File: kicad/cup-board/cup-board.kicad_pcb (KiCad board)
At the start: 4 copper layers, 0 parts

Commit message: [LIMA] cup PCB: ring outline (62/38 mm, centre 150,100), JLC 4-layer rules, netclasses
Outline drawn with KiCad's pcbnew API (Konnect has no circular Edge.Cuts
tool); DRC on the saved file: 0 violations.

Co-Authored-By: Claude Opus 5.5 <noreply@anthropic.com>
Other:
- board outline added: 62 x 62 mm
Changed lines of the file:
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@@
 (kicad_pcb
-	(version 20250610)
-	(generator "konnect")
+	(version 20260206)
+	(generator "pcbnew")
 	(generator_version "10.0")
 	(general
 		(thickness 1.6)
+		(legacy_teardrops no)
 	)
 	(paper "A4")
 	(layers
 		(0 "F.Cu" signal)
-		(31 "B.Cu" signal)
-		(32 "B.Adhes" user "B.Adhesive")
-		(33 "F.Adhes" user "F.Adhesive")
-		(34 "B.Paste" user)
-		(35 "F.Paste" user)
-		(36 "B.SilkS" user "B.Silkscreen")
-		(37 "F.SilkS" user "F.Silkscreen")
-		(38 "B.Mask" user)
-		(39 "F.Mask" user)
-		(40 "Dwgs.User" user "User.Drawings")
-		(41 "Cmts.User" user "User.Comments")
-		(44 "Edge.Cuts" user)
-		(45 "Margin" user)
-		(46 "B.CrtYd" user "B.Courtyard")
-		(47 "F.CrtYd" user "F.Courtyard")
-		(48 "B.Fab" user)
-		(49 "F.Fab" user)
-		(1 "In1.Cu" power)
-		(2 "In2.Cu" mixed)
+		(4 "In1.Cu" power)
+		(6 "In2.Cu" mixed)
+		(2 "B.Cu" signal)
+		(9 "F.Adhes" user "F.Adhesive")
+		(11 "B.Adhes" user "B.Adhesive")
+		(13 "F.Paste" user)
+		(15 "B.Paste" user)
+		(5 "F.SilkS" user "F.Silkscreen")
+		(7 "B.SilkS" user "B.Silkscreen")
+		(1 "F.Mask" user)
+		(3 "B.Mask" user)
+		(17 "Dwgs.User" user "User.Drawings")
+		(19 "Cmts.User" user "User.Comments")
+		(25 "Edge.Cuts" user)
+		(27 "Margin" user)
+		(31 "F.CrtYd" user "F.Courtyard")
+		(29 "B.CrtYd" user "B.Courtyard")
+		(35 "F.Fab" user)
+		(33 "B.Fab" user)
 	)
 	(setup
 		(pad_to_mask_clearance 0.05)
+		(allow_soldermask_bridges_in_footprints no)
+		(tenting
+			(front yes)
+			(back yes)
+		)
+		(covering
+			(front no)
+			(back no)
+		)
+		(plugging
+			(front no)
+			(back no)
+		)
+		(capping no)
+		(filling no)
+		(pcbplotparams
+			(layerselection 0x00000000_00000000_55555555_5755f5ff)
+			(plot_on_all_layers_selection 0x00000000_00000000_00000000_00000000)
+			(disableapertmacros no)
+			(usegerberextensions no)
+			(usegerberattributes yes)
+			(usegerberadvancedattributes yes)
+			(creategerberjobfile yes)
+			(dashed_line_dash_ratio 12)
+			(dashed_line_gap_ratio 3)
+			(svgprecision 4)
+			(plotframeref no)
+			(mode 1)
+			(useauxorigin no)
+			(pdf_front_fp_property_popups yes)
+			(pdf_back_fp_property_popups yes)
+			(pdf_metadata yes)
+			(pdf_single_document no)
+			(dxfpolygonmode yes)
+			(dxfimperialunits yes)
+			(dxfusepcbnewfont yes)
+			(psnegative no)
+			(psa4output no)
+			(plot_black_and_white yes)
+			(sketchpadsonfab no)
+			(plotpadnumbers no)
+			(hidednponfab no)
+			(sketchdnponfab yes)
+			(crossoutdnponfab yes)
+			(subtractmaskfromsilk no)
+			(outputformat 1)
+			(mirror no)
+			(drillshape 1)
+			(scaleselection 1)
+			(outputdirectory "")
+		)
 	)
-	(net 0 "")
+	(gr_circle
+		(center 150 100)
+		(end 169 100)
+		(stroke
+			(width 0.05)
+			(type default)
+		)
+		(fill no)
+		(layer "Edge.Cuts")
+	)
+	(gr_circle
+		(center 150 100)
+		(end 181 100)
+		(stroke
+			(width 0.05)
+			(type default)
+		)
+		(fill no)
+		(layer "Edge.Cuts")
+	)
+	(embedded_fonts no)
 )

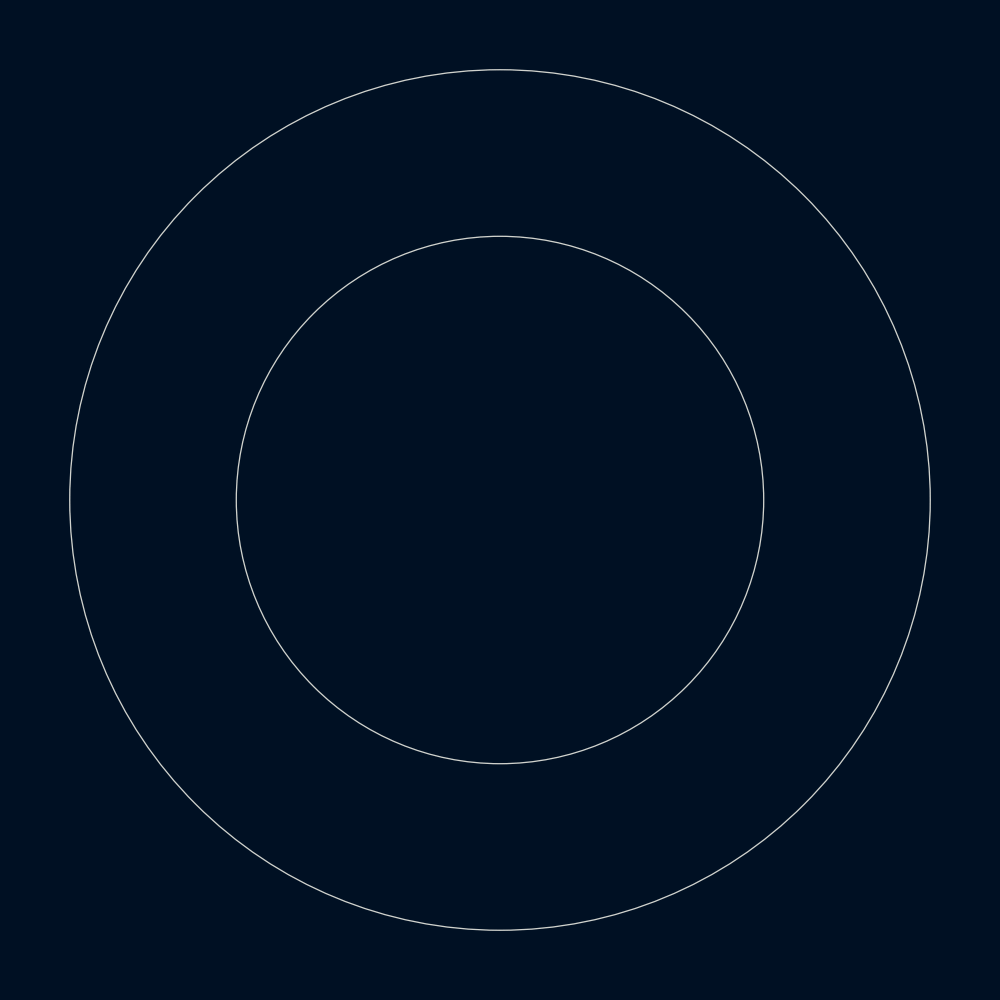
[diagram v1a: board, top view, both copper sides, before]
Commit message: [LIMA] cup PCB: ring enlarged to 68/38 mm (Peter); ring placement plan
62/38 put the parts at 57% courtyard fill on one side; Peter chose the
68/38 ring (single-sided, ~43%). Outer Edge.Cuts circle replaced r31 -> r34
via KiCad's pcbnew API (inner r19 unchanged).

doc/ring_placement.py packs the parts around the ring in signal order
(codec top, K2 right, A2B bottom, power/PPG left, mics upper right) and
checks exact courtyard corners against the ring and every pair for overlap:
359.9 deg used, 0 problems. Placement not yet applied (needs the schematic
sync with KiCad open).

Co-Authored-By: Claude Opus 5.5 <noreply@anthropic.com>
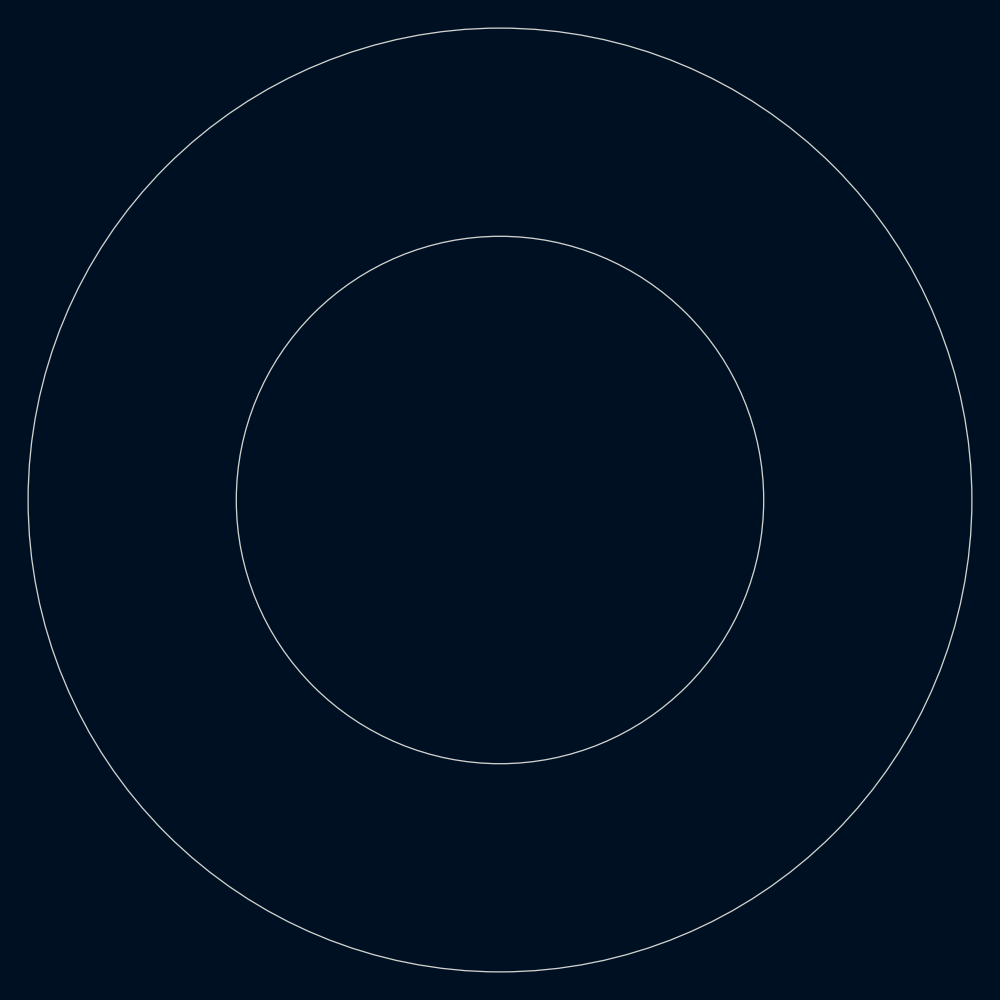
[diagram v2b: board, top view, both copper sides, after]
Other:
- board size 62 x 62 mm -> 68 x 68 mm
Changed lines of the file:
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@@
 	(gr_circle
 		(center 150 100)
-		(end 181 100)
+		(end 184 100)
 		(stroke
 			(width 0.05)

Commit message: [LIMA] cup PCB: 102 footprints synced from schematic (partial placement, pre-script)
Co-Authored-By: Claude Opus 5.5 <noreply@anthropic.com>
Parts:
- added C1: 100nF, Capacitor_SMD:C_0603_1608Metric, F.Cu at (6.48, 0.73)
- added C10: 1uF, Capacitor_SMD:C_0603_1608Metric, F.Cu at (6.48, 59.9)
- added C11: 1uF, Capacitor_SMD:C_0603_1608Metric, F.Cu at (6.48, 66.3)
- added C12: 330nF, Capacitor_SMD:C_0603_1608Metric, F.Cu at (6.48, 72.8)
- added C13: 12pF C0G, Capacitor_SMD:C_0603_1608Metric, F.Cu at (6.48, 79.2)
- added C14: 27pF C0G, Capacitor_SMD:C_0603_1608Metric, F.Cu at (6.48, 85.7)
- added C15: 27pF C0G, Capacitor_SMD:C_0603_1608Metric, F.Cu at (6.48, 92.2)
- added C16: 33nF, Capacitor_SMD:C_0603_1608Metric, F.Cu at (6.48, 98.6)
- added C17: 33nF, Capacitor_SMD:C_0603_1608Metric, F.Cu at (6.48, 105.1)
- added C18: 10nF, Capacitor_SMD:C_0603_1608Metric, F.Cu at (6.48, 111.5)
- added C19: 10nF, Capacitor_SMD:C_0603_1608Metric, F.Cu at (6.48, 118.0)
- added C2: 100nF, Capacitor_SMD:C_0603_1608Metric, F.Cu at (6.48, 7.19)
- added C20: 33nF, Capacitor_SMD:C_0603_1608Metric, F.Cu at (6.48, 124.5)
- added C21: 33nF, Capacitor_SMD:C_0603_1608Metric, F.Cu at (6.48, 130.9)
- added C22: 470nF, Capacitor_SMD:C_0603_1608Metric, F.Cu at (6.48, 137.4)
- added C23: 10uF 16V, Capacitor_SMD:C_0805_2012Metric, F.Cu at (6.70, 144.1)
- added C24: 33nF, Capacitor_SMD:C_0603_1608Metric, F.Cu at (6.48, 150.8)
- added C25: 15nF, Capacitor_SMD:C_0603_1608Metric, F.Cu at (6.48, 157.3)
- added C26: 3.3nF, Capacitor_SMD:C_0603_1608Metric, F.Cu at (6.48, 163.7)
- added C27: 12pF C0G, Capacitor_SMD:C_0603_1608Metric, F.Cu at (6.48, 170.2)
- added C28: 27pF C0G, Capacitor_SMD:C_0603_1608Metric, F.Cu at (6.48, 176.6)
- added C29: 33nF, Capacitor_SMD:C_0603_1608Metric, F.Cu at (6.48, 183.1)
- added C3: 10uF, Capacitor_SMD:C_0805_2012Metric, F.Cu at (6.70, 13.9)
- added C30: 10nF, Capacitor_SMD:C_0603_1608Metric, F.Cu at (6.48, 189.6)
- added C31: 10nF, Capacitor_SMD:C_0603_1608Metric, F.Cu at (6.48, 196.0)
- added C32: 33nF, Capacitor_SMD:C_0603_1608Metric, F.Cu at (6.48, 202.5)
- added C33: 33nF, Capacitor_SMD:C_0603_1608Metric, F.Cu at (6.48, 208.9)
- added C34: 33nF, Capacitor_SMD:C_0603_1608Metric, F.Cu at (6.48, 215.4)
- added C35: 100nF, Capacitor_SMD:C_0603_1608Metric, F.Cu at (6.48, 221.9)
- added C36: 4.7uF, Capacitor_SMD:C_0603_1608Metric, F.Cu at (6.48, 228.3)
- added C37: 100nF, Capacitor_SMD:C_0603_1608Metric, F.Cu at (6.48, 234.8)
- added C38: 4.7uF, Capacitor_SMD:C_0603_1608Metric, F.Cu at (6.48, 241.2)
- added C39: 100nF, Capacitor_SMD:C_0603_1608Metric, F.Cu at (6.48, 247.7)
- added C4: 100nF, Capacitor_SMD:C_0603_1608Metric, F.Cu at (6.48, 20.6)
- added C40: 100nF, Capacitor_SMD:C_0603_1608Metric, F.Cu at (6.48, 254.2)
- added C41: 10uF 16V, Capacitor_SMD:C_0805_2012Metric, F.Cu at (6.70, 260.9)
- added C42: 22uF, Capacitor_SMD:C_0805_2012Metric, F.Cu at (6.70, 267.8)
- added C43: 2.2uF 16V, Capacitor_SMD:C_0603_1608Metric, F.Cu at (6.48, 274.6)
- added C44: 2.2uF, Capacitor_SMD:C_0603_1608Metric, F.Cu at (6.48, 281.0)
- added C45: 2.2uF 16V, Capacitor_SMD:C_0603_1608Metric, F.Cu at (6.48, 287.5)
- added C46: 2.2uF, Capacitor_SMD:C_0603_1608Metric, F.Cu at (6.48, 293.9)
- added C47: 1uF, Capacitor_SMD:C_0603_1608Metric, F.Cu at (6.48, 300.4)
- added C48: 100nF, Capacitor_SMD:C_0603_1608Metric, F.Cu at (6.48, 306.8)
- added C5: 100nF, Capacitor_SMD:C_0603_1608Metric, F.Cu at (6.48, 27.1)
- added C6: 10uF, Capacitor_SMD:C_0805_2012Metric, F.Cu at (6.70, 33.8)
- added C7: 1uF, Capacitor_SMD:C_0603_1608Metric, F.Cu at (6.48, 40.5)
- added C8: 1uF, Capacitor_SMD:C_0603_1608Metric, F.Cu at (6.48, 46.9)
- added C9: 1uF, Capacitor_SMD:C_0603_1608Metric, F.Cu at (6.48, 53.4)
- added D1: ZLLS400, Diode_SMD:D_SOD-323, F.Cu at (131.0, 92.9)
- added FB1: 1000R@100MHz, Inductor_SMD:L_0603_1608Metric, F.Cu at (137.4, 119.5)
- added FB2: 1000R@100MHz, Inductor_SMD:L_0603_1608Metric, F.Cu at (136.5, 120.9)
- added FB3: 1000R@100MHz, Inductor_SMD:L_0603_1608Metric, F.Cu at (130.7, 112.8)
- added FB4: 1000R@100MHz, Inductor_SMD:L_0603_1608Metric, F.Cu at (129.3, 113.7)
- added FL1: 2600R@100MHz CMC, Inductor_SMD:L_CommonModeChoke_Coilank_ACM3216, F.Cu at (142.8, 125.5)
- added FL2: 2600R@100MHz CMC, Inductor_SMD:L_CommonModeChoke_Coilank_ACM3216, F.Cu at (127.3, 110.2)
- added H1: M2, MountingHole:MountingHole_2.2mm_M2, F.Cu at (176.4, 98.2)
- added H2: M2, MountingHole:MountingHole_2.2mm_M2, F.Cu at (128.0, 85.2)
- added H3: M2, MountingHole:MountingHole_2.2mm_M2, F.Cu at (153.7, 73.8)
- added J2: EARCUP_SPKR, Connector_JST:JST_GH_SM02B-GHS-TB_1x02-1MP_P1.25mm_Horizontal, F.Cu at (165.1, 126.9)
- added J7: CUP_IN (A2B + panel audio, mates audio J3), Connector_JST:JST_GH_SM04B-GHS-TB_1x04-1MP_P1.25mm_Horizontal, F.Cu at (156.3, 130.1)
- added J8: CUP_OUT (A2B to next cup), Connector_JST:JST_GH_SM02B-GHS-TB_1x02-1MP_P1.25mm_Horizontal, F.Cu at (121.1, 89.3)
- added L1: 180nH, Inductor_SMD:L_0603_1608Metric, F.Cu at (140.3, 121.1)
- added L2: 180nH, Inductor_SMD:L_0603_1608Metric, F.Cu at (139.6, 122.6)
- added L3: 3.3uH, Inductor_SMD:L_1210_3225Metric, F.Cu at (148.2, 123.1)
- added L4: 3.3uH, Inductor_SMD:L_1210_3225Metric, F.Cu at (147.9, 126.4)
- added L5: 3.3uH, Inductor_SMD:L_1210_3225Metric, F.Cu at (126.9, 101.8)
- added L6: 3.3uH, Inductor_SMD:L_1210_3225Metric, F.Cu at (123.6, 102.1)
- added L7: 180nH, Inductor_SMD:L_0603_1608Metric, F.Cu at (126.5, 115.5)
- added L8: 180nH, Inductor_SMD:L_0603_1608Metric, F.Cu at (125.1, 116.4)
- added L9: 2.2uH, Inductor_SMD:L_1008_2520Metric, F.Cu at (128.7, 79.2)
- added MK1: IM73A135V01, Infineon:Infineon_PG-LLGA-5_4x3mm_IM73A135_IM72D128, F.Cu at (177.3, 92.2)
- added MK2: IM73A135V01, Infineon:Infineon_PG-LLGA-5_4x3mm_IM73A135_IM72D128, F.Cu at (173.7, 93.2)
- added MK3: IM72D128VV01, Infineon:Infineon_PG-LLGA-5_4x3mm_IM73A135_IM72D128, F.Cu at (148.4, 72.7)
- added Q1: AO3401A, Package_TO_SOT_SMD:SOT-23, F.Cu at (127.4, 97.1)
- added Q2: MMBT3904, Package_TO_SOT_SMD:SOT-23, F.Cu at (160.3, 118.4)
- added R1: 10k, Resistor_SMD:R_0603_1608Metric, F.Cu at (6.48, 544.1)
- added R10: 120R, Resistor_SMD:R_0603_1608Metric, F.Cu at (6.48, 602.3)
- added R11: 33k, Resistor_SMD:R_0603_1608Metric, F.Cu at (6.48, 608.7)
- added R12: 1R 1206, Resistor_SMD:R_1206_3216Metric, F.Cu at (7.28, 615.6)
- added R13: 3.3k, Resistor_SMD:R_0603_1608Metric, F.Cu at (6.48, 622.5)
- added R14: 1k, Resistor_SMD:R_0603_1608Metric, F.Cu at (6.48, 628.9)
- added R15: 120R, Resistor_SMD:R_0603_1608Metric, F.Cu at (6.48, 635.4)
- added R16: 120R, Resistor_SMD:R_0603_1608Metric, F.Cu at (6.48, 641.8)
- added R17: 2.2k, Resistor_SMD:R_0603_1608Metric, F.Cu at (6.48, 648.3)
- added R18: 100k, Resistor_SMD:R_0603_1608Metric, F.Cu at (6.48, 654.8)
- added R2: 10k, Resistor_SMD:R_0603_1608Metric, F.Cu at (6.48, 550.6)
- added R3: 10k, Resistor_SMD:R_0603_1608Metric, F.Cu at (6.48, 557.1)
- added R4: 10k, Resistor_SMD:R_0603_1608Metric, F.Cu at (6.48, 563.5)
- added R5: 10k, Resistor_SMD:R_0603_1608Metric, F.Cu at (6.48, 570.0)
- added R6: 22k, Resistor_SMD:R_0603_1608Metric, F.Cu at (6.48, 576.4)
- added R7: 680, Resistor_SMD:R_0603_1608Metric, F.Cu at (6.48, 582.9)
- added R8: 680, Resistor_SMD:R_0603_1608Metric, F.Cu at (6.48, 589.4)
- added R9: 120R, Resistor_SMD:R_0603_1608Metric, F.Cu at (6.48, 595.8)
- added U1: ADAU1861, AnalogDevices:AD_LFCSP-SS-64-1EP_9x9mm_P0.5mm_EP6.3x6.3mm_CS-64-2, F.Cu at (165.4, 79.4)
- added U2: LSM6DSV16BX, Package_LGA:LGA-14_3x2.5mm_P0.5mm_LayoutBorder3x4y, F.Cu at (171.5, 89.2)
- added U3: MAXM86161, AnalogDevices:Maxim_OLGA-14_2.9x4.3mm_P0.6mm_F142A4_MAXM86161, F.Cu at (143.5, 75.2)
- added U4: AQW612S, Panasonic:Panasonic_GU-SOP8_4.4x9.37mm_P2.54mm_AQW61xS, F.Cu at (175.6, 106.8)
- added U5: AQW612S, Panasonic:Panasonic_GU-SOP8_4.4x9.37mm_P2.54mm_AQW61xS, F.Cu at (170.2, 117.2)
- added U6: AD2428WBCPZ (sub-node), Package_DFN_QFN:QFN-32-1EP_5x5mm_P0.5mm_EP3.6x3.6mm_ThermalVias, F.Cu at (131.4, 118.8)
- added U7: TPS62161DSG (1V8), Package_SON:WSON-8-1EP_2x2mm_P0.5mm_EP0.9x1.6mm_ThermalVias, F.Cu at (130.7, 81.2)
- added U8: ADP7118AUJZ-3.3-R7 (3V3_MIC), Package_TO_SOT_SMD:TSOT-23-5, F.Cu at (133.6, 77.8)
- added U9: ADP7118AUJZ-3.3-R7 (VLED), Package_TO_SOT_SMD:TSOT-23-5, F.Cu at (139.5, 78.7)

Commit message: [LIMA] cup PCB: all 102 parts placed on the 68/38 ring, DRC 0 errors
Synced via Konnect, then positions and tangential angles applied with
KiCad's pcbnew API (KiCad closed, Peter approved) because Konnect's IPC
refuses non-90 deg rotation of rounded-rect-pad footprints. J2/J7/J8 pulled
in 0.16-0.29 mm so their MP tabs clear the curved edge by 0.5 mm.

kicad-cli DRC on the saved file: 0 errors (250 unconnected = unrouted),
schematic parity 0. Scripts and placement table in kicad/cup-board/doc/.

Co-Authored-By: Claude Opus 5.5 <noreply@anthropic.com>
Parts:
- moved R18 560.0 mm to (173.8, 120.3), turned to 49.53 degrees
- moved R17 557.7 mm to (166.5, 114.1), turned to 49.53 degrees
- moved R16 542.1 mm to (122.5, 112.3), turned to -65.87 degrees
- moved R14 538.5 mm to (119.4, 102.4), turned to -85.55 degrees
- moved R15 536.8 mm to (124.0, 111.6), turned to -65.87 degrees
- moved R13 532.7 mm to (121.1, 102.2), turned to -85.55 degrees
- moved R12 531.8 mm to (122.8, 96.5), turned to -97.39 degrees
- moved R11 525.5 mm to (124.8, 96.7), turned to -97.39 degrees
- moved R6 520.7 mm to (173.7, 83.3), turned to 125.19 degrees
- moved R5 513.3 mm to (172.3, 84.2), turned to 125.19 degrees
- moved R8 511.7 mm to (180.2, 108.1), turned to 75.08 degrees
- moved R4 505.8 mm to (171.0, 85.2), turned to 125.19 degrees
- moved R7 504.9 mm to (171.0, 105.6), turned to 75.08 degrees
- moved R3 504.7 mm to (142.4, 71.0), turned to -165.35 degrees
- moved R10 497.9 mm to (143.3, 123.6), turned to -15.76 degrees
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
